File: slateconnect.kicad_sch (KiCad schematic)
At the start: 45 parts, among them CN5 DF40C-40DP-0.4V, J6 Conn_02x08_Odd_Even, U10 TS3A24159DGSR, U55 TCA9534APWR, U56 TS3A24159DGSR, U57 TS3A24159DGSR, U58 TS3A24159DGSR, U59 TPS259470ARPWR, U60 TPS259470ARPWR, U61 TCA9534APWR

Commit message: finished BOM, replaced discontinued parts, added missing footprints, updated schematics and libraries
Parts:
- C143, C146: footprint (none) -> Capacitor_SMD:C_0603_1608Metric; LCSC Part (none) -> C1613; MPN (none) -> CL10B332KB8NNNC
- C144, C18: LCSC Part (none) -> C15849; MPN CL10B105KA8NNNC -> CL10A105KB8NNNC
- C145, C20: LCSC Part (none) -> C380317; MPN CL10A106KP8NNNC -> TCC0603X5R106M160CT
- C148, C149, C151, C152, C153, C154: LCSC Part (none) -> C1591
- J6: DigiKey Part (none) -> 151-395-016-520-202-ND; MPN EDAC 395-016-520-202 -> 395-016-520-202; Manufacturer DigiKey -> EDAC Inc.
- R30, R77, R78, R79, R80, R81, R82, R83: LCSC Part (none) -> C23345; MPN RC0603FR-0722RL -> 0603WAF220JT5E
- R84, R88, R90, R94: LCSC Part (none) -> C25804; MPN RC0603FR-0710KL -> 0603WAF1002T5E
- R85, R87, R91, R92: LCSC Part (none) -> C25803; MPN RC0603FR-07100KL -> 0603WAF1003T5E
- R86, R93: LCSC Part (none) -> C23048; MPN RC0603FR-07402KL -> 0603WAF4023T5E
- R89, R95: LCSC Part (none) -> C22978; MPN RC0603FR-073K3L -> 0603WAF3301T5E

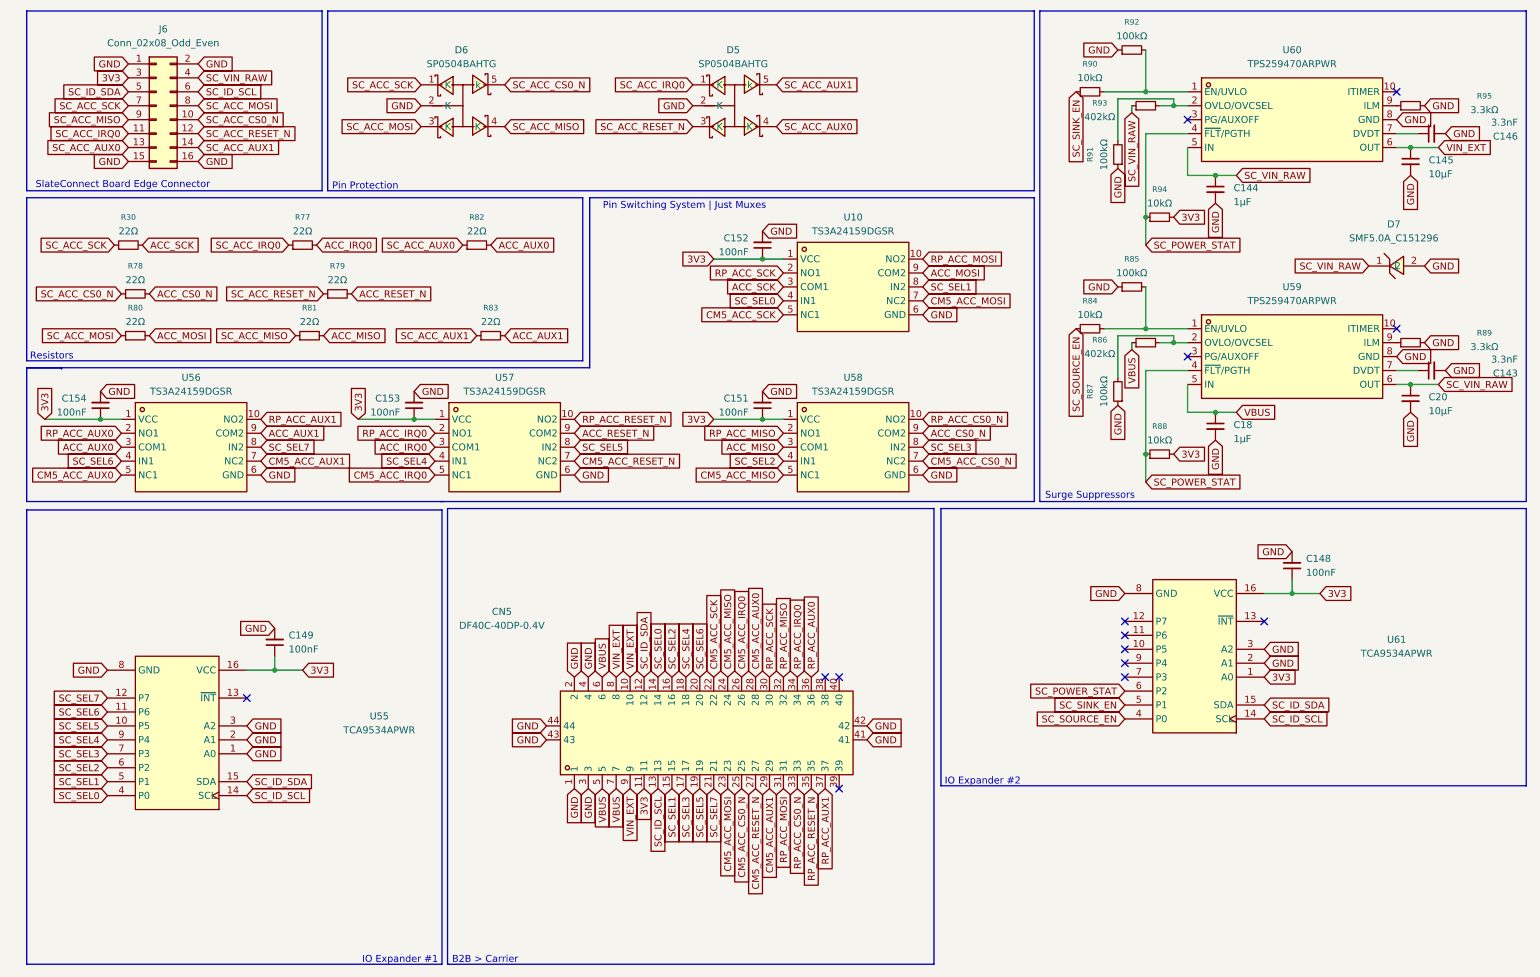
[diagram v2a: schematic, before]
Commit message: imported footprints and 3d models, replaced obsolete components, finished schematic audit, wired new usb hub and flash chip + more, removed stale nets
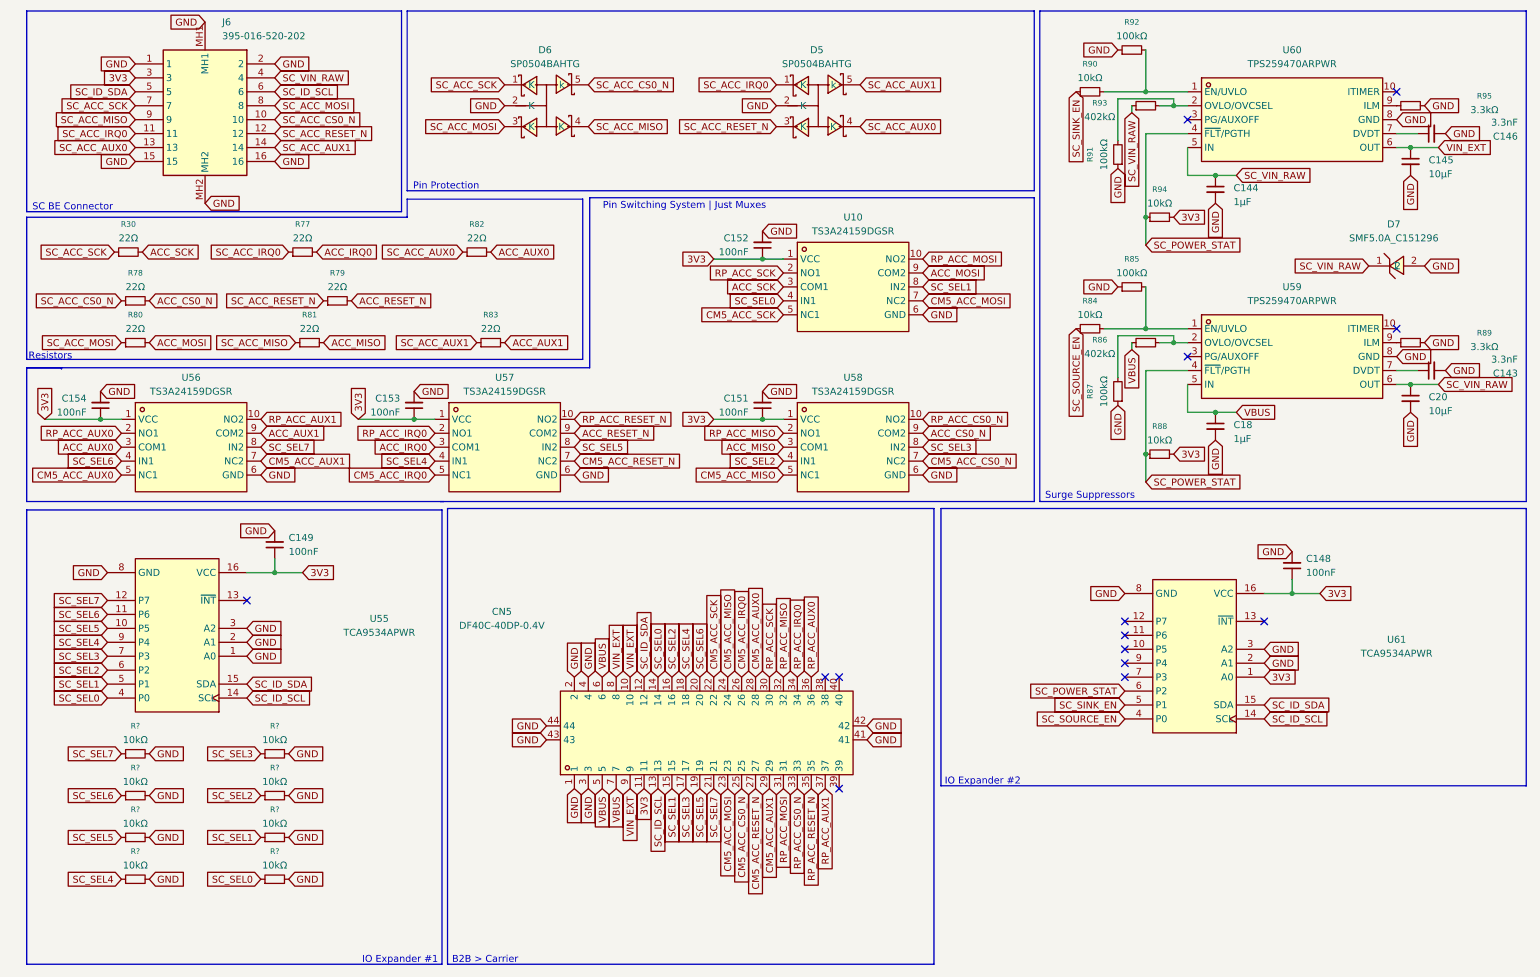
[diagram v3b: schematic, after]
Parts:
- removed J6: Conn_02x08_Odd_Even, symbol Connector_Generic:Conn_02x08_Odd_Even
- added J6: 395-016-520-202, slate113:395016520202, symbol slate113:395-016-520-202
- added R? (x8): 10kΩ, Resistor_SMD:R_0603_1608Metric, symbol Device:R_Small
- C144, C18: LCSC Part C15849 -> C92848; MPN CL10A105KB8NNNC -> UMK107BJ105KA-T; Manufacturer Samsung Electro-Mechanics -> Taiyo Yuden
- R84, R88, R90, R94: LCSC Part C25804 -> C840630; MPN 0603WAF1002T5E -> CR0603-FX-1002ELF; Manufacturer Yageo -> Bourns
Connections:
- net 3V3: now also J6.3
- net GND: now also J6.1, J6.15, J6.16, J6.2, J6.MH1, J6.MH2, R?.2, R?.2, R?.2, R?.2, R?.2, R?.2, R?.2, R?.2
- net SC_ACC_AUX0: now also J6.13
- net SC_ACC_AUX1: now also J6.14
- net SC_ACC_CS0_N: now also J6.10
- net SC_ACC_IRQ0: now also J6.11
- net SC_ACC_MISO: now also J6.9
- net SC_ACC_MOSI: now also J6.8
- net SC_ACC_RESET_N: now also J6.12
- net SC_ACC_SCK: now also J6.7
- net SC_ID_SCL: now also J6.6
- net SC_ID_SDA: now also J6.5
- net SC_SEL0: now also R?.1
- net SC_SEL1: now also R?.1
- net SC_SEL2: now also R?.1
- net SC_SEL3: now also R?.1
- net SC_SEL4: now also R?.1
- net SC_SEL5: now also R?.1
- net SC_SEL6: now also R?.1
- net SC_SEL7: now also R?.1
- net SC_VIN_RAW: now also J6.4
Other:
- note added: "SC BE Connector"
- note removed: "SlateConnect Board Edge Connector"
- moved on the sheet: C149, D5, D6, R30, R77, R78, R79, R80, R81, R82, R83, U55

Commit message: configured 8-layer pcb with micro vias, finished power mezzanine routing, completed io port, started work on slateconnect mezzanine
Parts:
- gave numbers to parts that had none: 8
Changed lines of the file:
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@@
 		(dnp no)
 		(fields_autoplaced yes)
-		(property "Reference" "R?"
+		(property "Reference" "R137"
 			(at 33.02 166.37 90)
 			(show_name no)
@@
 			(project "slate113"
 				(path "/45225493-9b42-42d2-b0ee-1bf1204de834"
-					(reference "R?")
+					(reference "R137")
 					(unit 1)
 				)
@@
 		(dnp no)
 		(fields_autoplaced yes)
-		(property "Reference" "R?"
+		(property "Reference" "R140"
 			(at 58.42 158.75 90)
 			(show_name no)
@@
 			(project "slate113"
 				(path "/45225493-9b42-42d2-b0ee-1bf1204de834"
-					(reference "R?")
+					(reference "R140")
 					(unit 1)
 				)
@@
 		(dnp no)
 		(fields_autoplaced yes)
-		(property "Reference" "R?"
+		(property "Reference" "R135"
 			(at 33.02 151.13 90)
 			(show_name no)
@@
 			(project "slate113"
 				(path "/45225493-9b42-42d2-b0ee-1bf1204de834"
-					(reference "R?")
+					(reference "R135")
 					(unit 1)
 				)
@@
 		(dnp no)
 		(fields_autoplaced yes)
-		(property "Reference" "R?"
+		(property "Reference" "R136"
 			(at 33.02 158.75 90)
 			(show_name no)
@@
 			(project "slate113"
 				(path "/45225493-9b42-42d2-b0ee-1bf1204de834"
-					(reference "R?")
+					(reference "R136")
 					(unit 1)
 				)
@@
 		(dnp no)
 		(fields_autoplaced yes)
-		(property "Reference" "R?"
+		(property "Reference" "R138"
 			(at 58.42 143.51 90)
 			(show_name no)
@@
 			(project "slate113"
 				(path "/45225493-9b42-42d2-b0ee-1bf1204de834"
-					(reference "R?")
+					(reference "R138")
 					(unit 1)
 				)
@@
 		(dnp no)
 		(fields_autoplaced yes)
-		(property "Reference" "R?"
+		(property "Reference" "R139"
 			(at 58.42 151.13 90)
 			(show_name no)
@@
 			(project "slate113"
 				(path "/45225493-9b42-42d2-b0ee-1bf1204de834"
-					(reference "R?")
+					(reference "R139")
 					(unit 1)
 				)
@@
 			(show_name no)
 			(do_not_autoplace no)
-			(effects (font (size 1.27 1.27)) (justify left top))
+			(effects
+				(font
+					(size 1.27 1.27)
+				)
+				(justify left top)
+			)
 		)
 		(property "Manufacturer" "EDAC Inc."
@@
 			(show_name no)
 			(do_not_autoplace no)
-			(effects (font (size 1.27 1.27)) (justify left top))
+			(effects
+				(font
+					(size 1.27 1.27)
+				)
+				(justify left top)
+			)
 		)
 		(property "DigiKey Part" "151-395-016-520-202-ND"
@@
 			(show_name no)
 			(do_not_autoplace no)
-			(effects (font (size 1.27 1.27)) (justify left top))
+			(effects
+				(font
+					(size 1.27 1.27)
+				)
+				(justify left top)
+			)
 		)
 		(pin "11"
@@
 		(dnp no)
 		(fields_autoplaced yes)
-		(property "Reference" "R?"
+		(property "Reference" "R134"
 			(at 33.02 143.51 90)
 			(show_name no)
@@
 			(project "slate113"
 				(path "/45225493-9b42-42d2-b0ee-1bf1204de834"
-					(reference "R?")
+					(reference "R134")
 					(unit 1)
 				)
@@
 		(dnp no)
 		(fields_autoplaced yes)
-		(property "Reference" "R?"
+		(property "Reference" "R141"
 			(at 58.42 166.37 90)
 			(show_name no)
@@
 			(project "slate113"
 				(path "/45225493-9b42-42d2-b0ee-1bf1204de834"
-					(reference "R?")
+					(reference "R141")
 					(unit 1)
 				)

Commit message: finished m.2 board and copper pours, completed antenna bracket and power board, finished slateconnect board, reorganized libraries
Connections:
- net SC_SEL0: no longer CN5.14
- net SC_SEL1: no longer CN5.15
- net SC_SEL2: no longer CN5.16
- net SC_SEL3: no longer CN5.17
- net SC_SEL4: no longer CN5.18
- net SC_SEL5: no longer CN5.19
- net SC_SEL6: no longer CN5.20
- net SC_SEL7: no longer CN5.21
- no-connect marks 14 -> 22
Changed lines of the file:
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@@
 	)
 	(no_connect
+		(at 138.43 154.94)
+	)
+	(no_connect
 		(at 158.75 134.62)
 	)
@@
 	)
 	(no_connect
+		(at 128.27 134.62)
+	)
+	(no_connect
 		(at 213.36 132.08)
 	)
@@
 	)
 	(no_connect
+		(at 130.81 154.94)
+	)
+	(no_connect
 		(at 213.36 127)
 	)
@@
 	)
 	(no_connect
+		(at 130.81 134.62)
+	)
+	(no_connect
+		(at 135.89 154.94)
+	)
+	(no_connect
+		(at 135.89 134.62)
+	)
+	(no_connect
 		(at 161.29 134.62)
 	)
@@
 		(at 213.36 129.54)
 	)
+	(no_connect
+		(at 133.35 134.62)
+	)
+	(no_connect
+		(at 133.35 154.94)
+	)
 	(wire
 		(pts
@@
 		)
 	)
-	(global_label "SC_SEL6"
-		(shape input)
-		(at 135.89 134.62 90)
-		(fields_autoplaced yes)
-		(effects
-			(font
-				(size 1.27 1.27)
-			)
-			(justify left)
-		)
-		(property "Intersheetrefs" "${INTERSHEET_REFS}"
-			(at 135.89 123.5916 90)
-			(hide yes)
-			(show_name no)
-			(do_not_autoplace no)
-			(effects
-				(font
-					(size 1.27 1.27)
-				)
-				(justify left)
-			)
-		)
-	)
 	(global_label "GND"
 		(shape input)
@@
 		)
 	)
-	(global_label "SC_SEL3"
-		(shape input)
-		(at 133.35 154.94 270)
-		(fields_autoplaced yes)
-		(effects
-			(font
-				(size 1.27 1.27)
-			)
-			(justify right)
-		)
-		(property "Intersheetrefs" "${INTERSHEET_REFS}"
-			(at 133.35 165.9684 90)
-			(hide yes)
-			(show_name no)
-			(do_not_autoplace no)
-			(effects
-				(font
-					(size 1.27 1.27)
-				)
-				(justify right)
-			)
-		)
-	)
 	(global_label "GND"
 		(shape input)
@@
 		)
 	)
-	(global_label "SC_SEL2"
-		(shape input)
-		(at 130.81 134.62 90)
-		(fields_autoplaced yes)
-		(effects
-			(font
-				(size 1.27 1.27)
-			)
-			(justify left)
-		)
-		(property "Intersheetrefs" "${INTERSHEET_REFS}"
-			(at 130.81 123.5916 90)
-			(hide yes)
-			(show_name no)
-			(do_not_autoplace no)
-			(effects
-				(font
-					(size 1.27 1.27)
-				)
-				(justify left)
-			)
-		)
-	)
 	(global_label "GND"
 		(shape input)
@@
 		)
 	)
-	(global_label "SC_SEL5"
-		(shape input)
-		(at 135.89 154.94 270)
-		(fields_autoplaced yes)
-		(effects
-			(font
-				(size 1.27 1.27)
-			)
-			(justify right)
-		)
-		(property "Intersheetrefs" "${INTERSHEET_REFS}"
-			(at 135.89 165.9684 90)
-			(hide yes)
-			(show_name no)
-			(do_not_autoplace no)
-			(effects
-				(font
-					(size 1.27 1.27)
-				)
-				(justify right)
-			)
-		)
-	)
 	(global_label "CM5_ACC_AUX1"
 		(shape input)
@@
 		)
 	)
-	(global_label "SC_SEL4"
-		(shape input)
-		(at 133.35 134.62 90)
-		(fields_autoplaced yes)
-		(effects
-			(font
-				(size 1.27 1.27)
-			)
-			(justify left)
-		)
-		(property "Intersheetrefs" "${INTERSHEET_REFS}"
-			(at 133.35 123.5916 90)
-			(hide yes)
-			(show_name no)
-			(do_not_autoplace no)
-			(effects
-				(font
-					(size 1.27 1.27)
-				)
-				(justify left)
-			)
-		)
-	)
 	(global_label "SC_SEL7"
 		(shape input)
@@
 		)
 	)
-	(global_label "SC_SEL7"
-		(shape input)
-		(at 138.43 154.94 270)
-		(fields_autoplaced yes)
-		(effects
-			(font
-				(size 1.27 1.27)
-			)
-			(justify right)
-		)
-		(property "Intersheetrefs" "${INTERSHEET_REFS}"
-			(at 138.43 165.9684 90)
-			(hide yes)
-			(show_name no)
-			(do_not_autoplace no)
-			(effects
-				(font
-					(size 1.27 1.27)
-				)
-				(justify right)
-			)
-		)
-	)
 	(global_label "3V3"
 		(shape input)
@@
 		)
 	)
-	(global_label "SC_SEL0"
-		(shape input)
-		(at 128.27 134.62 90)
-		(fields_autoplaced yes)
-		(effects
-			(font
-				(size 1.27 1.27)
-			)
-			(justify left)
-		)
-		(property "Intersheetrefs" "${INTERSHEET_REFS}"
-			(at 128.27 123.5916 90)
-			(hide yes)
-			(show_name no)
-			(do_not_autoplace no)
-			(effects
-				(font
-					(size 1.27 1.27)
-				)
-				(justify left)
-			)
-		)
-	)
 	(global_label "3V3"
 		(shape input)
@@
 			(hide yes)
 			(show_name no)
-			(do_not_autoplace no)
-			(effects
-				(font
-					(size 1.27 1.27)
-				)
-				(justify right)
-			)
-		)
-	)
-	(global_label "SC_SEL1"
-		(shape input)
-		(at 130.81 154.94 270)
-		(fields_autoplaced yes)
-		(effects
-			(font
-				(size 1.27 1.27)
-			)
-			(justify right)
-		)
-		(property "Intersheetrefs" "${INTERSHEET_REFS}"
-			(at 130.81 165.9684 90)
-			(hide yes)
-			(show_name no)
